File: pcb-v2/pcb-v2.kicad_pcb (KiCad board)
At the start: 2 copper layers, 31 x 57.9 mm, 5 parts, among them J1 Conn_02x20_Odd_Even, J2 Conn_01x07_Socket, J3 Screw_Terminal_01x03, J4 Screw_Terminal_01x02

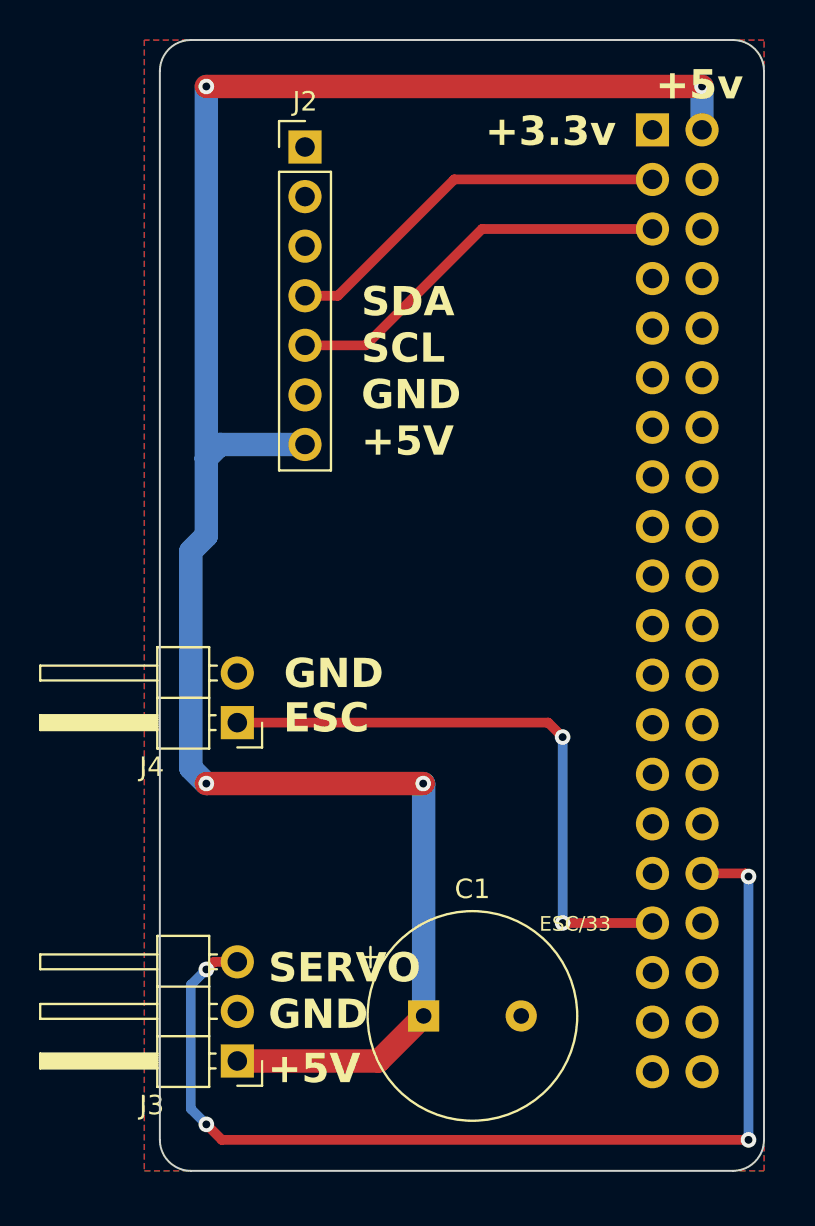
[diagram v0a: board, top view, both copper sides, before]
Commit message: updated silkscreen
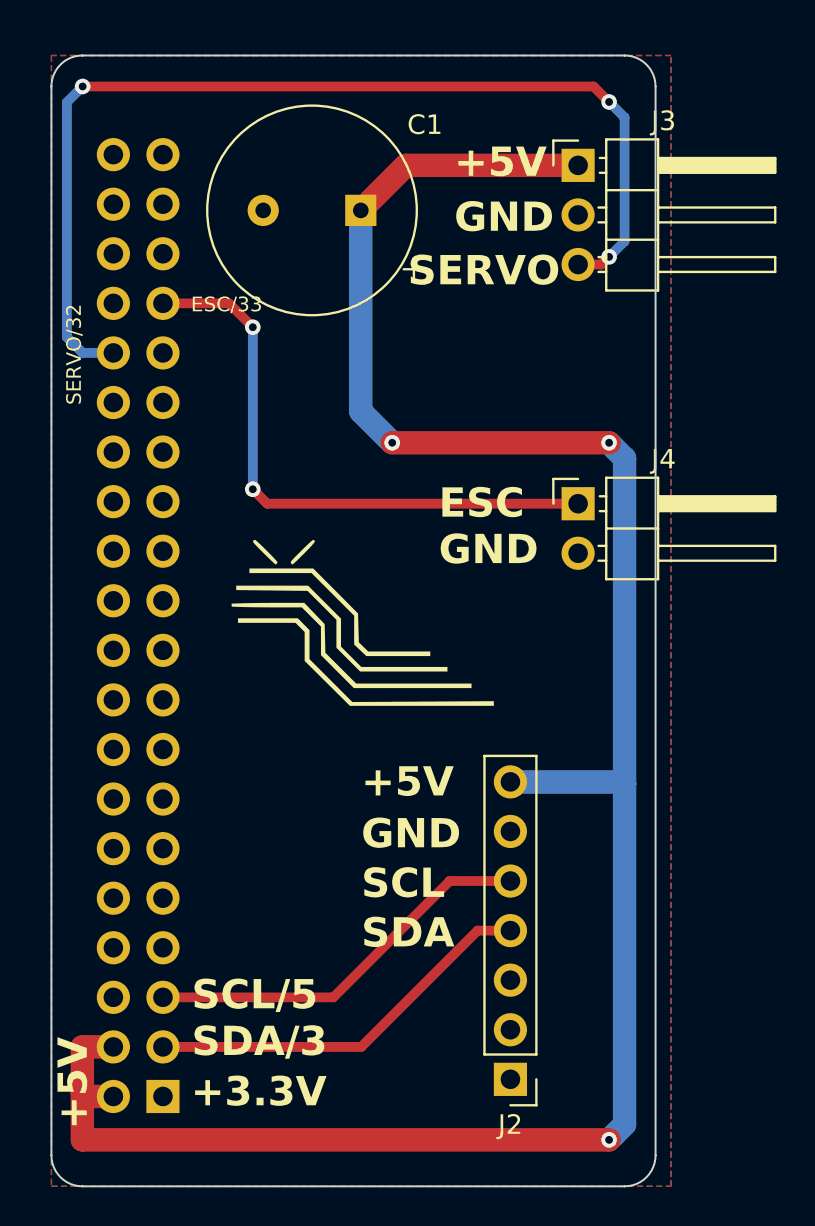
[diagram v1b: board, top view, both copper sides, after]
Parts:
- added G***: LOGO, LOGO, F.Cu at (193.0, 110.0)
- added G***: LOGO, LOGO, B.Cu at (197.2, 114.2)
- moved J1 55.5 mm to (182.7, 134.3), turned to 0 degrees
- moved J3 49.1 mm to (204.0, 86.6), turned to 0 degrees
- moved J2 48.9 mm to (200.5, 133.4), turned to 180 degrees
- moved C1 41.4 mm to (192.9, 88.9), turned to 180 degrees
- moved J4 20.8 mm to (204.0, 103.9), turned to 0 degrees
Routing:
- net +5V: track 102.9 -> 113.0 mm, vias 4 -> 3
- net SERVO: track 54.9 -> 53.8 mm, vias 4 -> 3
- net ESC: track 31.1 -> 30.4 mm
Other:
- board text added: "+"
- board text added: "+3.3V"
- board text added: "-"
- board text added: "SCL/5"
- board text added: "SDA/3"
- board text added: "SERVO/32"
- board text removed: "+3.3v"
- board text removed: "+5v"
